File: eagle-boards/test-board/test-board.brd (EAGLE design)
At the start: 120.6 x 30.1 mm, 17 parts

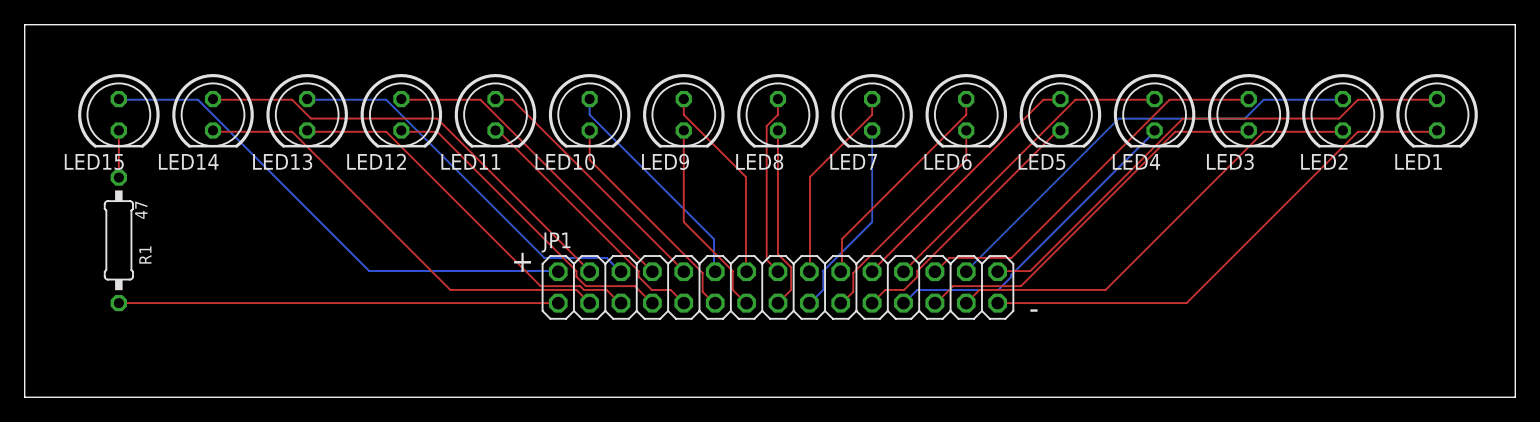
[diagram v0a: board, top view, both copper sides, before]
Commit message: Update the test board.
The new revision is smaller, and reports the connector on the bottom side as expected.
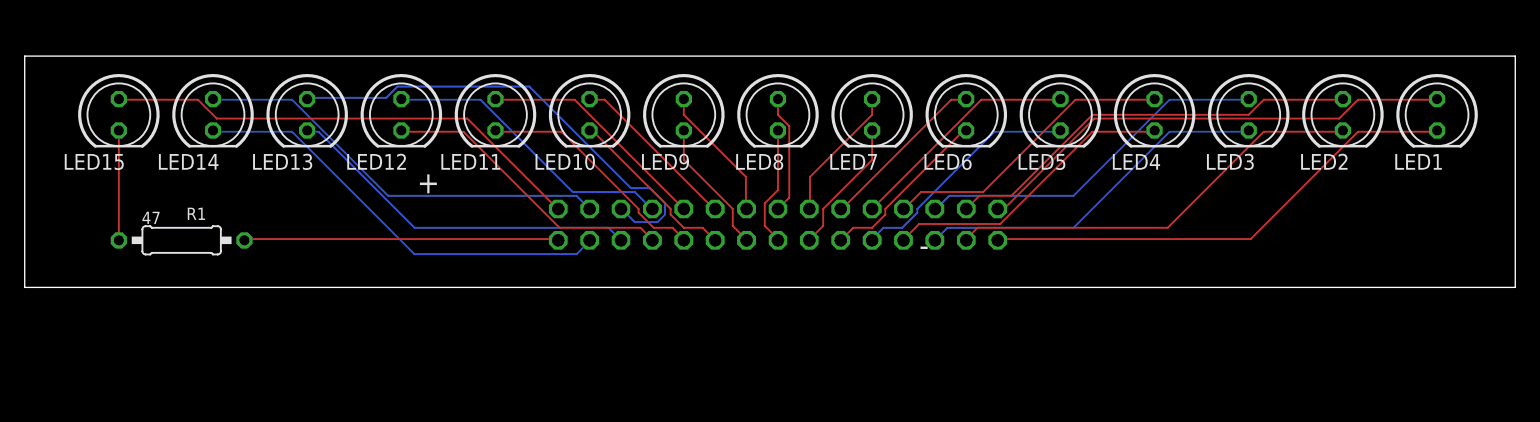
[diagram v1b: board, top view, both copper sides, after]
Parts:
- removed JP1: (no value), pinhead:2X15
- added JP2: (no value), pinhead:2X15
- moved R1 5.08 mm to (12.7, 12.7), turned to 0 degrees
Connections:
- net N$1: now also JP2.2; no longer JP1.1
- net N$10: now also JP2.24; no longer JP1.23
- net N$11: now also JP2.22; no longer JP1.21
- net N$12: now also JP2.20; no longer JP1.19
- net N$13: now also JP2.18; no longer JP1.17
- net N$14: now also JP2.16; no longer JP1.15
- net N$15: now also JP2.14; no longer JP1.13
- net N$16: now also JP2.1; no longer JP1.2
- net N$17: now also JP2.3; no longer JP1.4
- net N$18: now also JP2.5; no longer JP1.6
- net N$19: now also JP2.7; no longer JP1.8
- net N$2: now also JP2.4; no longer JP1.3
- net N$20: now also JP2.9; no longer JP1.10
- net N$21: now also JP2.11; no longer JP1.12
- net N$22: now also JP2.29; no longer JP1.30
- net N$23: now also JP2.27; no longer JP1.28
- net N$24: now also JP2.25; no longer JP1.26
- net N$25: now also JP2.23; no longer JP1.24
- net N$26: now also JP2.21; no longer JP1.22
- net N$27: now also JP2.19; no longer JP1.20
- net N$28: now also JP2.17; no longer JP1.18
- net N$29: now also JP2.15; no longer JP1.16
- net N$3: now also JP2.6; no longer JP1.5
- net N$30: now also JP2.13; no longer JP1.14
- net N$4: now also JP2.8; no longer JP1.7
- net N$5: now also JP2.10; no longer JP1.9
- net N$6: now also JP2.12; no longer JP1.11
- net N$7: now also JP2.30; no longer JP1.29
- net N$8: now also JP2.28; no longer JP1.27
- net N$9: now also JP2.26; no longer JP1.25
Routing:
- net N$1: track 35.6 -> 25.5 mm
- net N$18: track 31.2 -> 38.5 mm
- net N$13: track 16.1 -> 11.0 mm
- net N$15: track 16.1 -> 11.0 mm
- net N$32: track 3.81 -> 8.89 mm
- net N$29: track 14.7 -> 9.65 mm
- net N$14: track 14.9 -> 9.77 mm
- net N$30: track 16.1 -> 11.0 mm
- net N$28: track 16.1 -> 11.0 mm
- net N$21: track 18.2 -> 13.9 mm
- net N$27: track 18.2 -> 13.9 mm
- net N$6: track 18.2 -> 14.2 mm
- net N$12: track 18.2 -> 14.2 mm
- net N$4: track 26.4 -> 24.1 mm
- net N$10: track 26.3 -> 24.1 mm
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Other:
- board size 120.6 x 30.1 mm -> 120.6 x 18.7 mm
- board text added: "Birch Books Smart Home - Test Board rev. 2 Copyright © 2020 Diego Elio Pettenò flameeyes.com/p/birch-books Licensed under MIT License"
- board text removed: "Birch Books Smart Home - Test Board rev. 1a Copyright © 2020 Diego Elio Pettenò flameeyes.com/p/birch-books Licensed under MIT License"
